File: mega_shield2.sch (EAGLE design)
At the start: 36 parts, among them IC1 L298, IC2 LM2937ET-5V, J2 Mega R3, M1_M2 1X2-3.5MM, M3_M4 1X2-3.5MM

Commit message: Added 6 pin motor headers
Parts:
- removed M1_M2, M3_M4: 1X2-3.5MM, adafruit:1X2-3.5MM
- added JP1: MOTOR1_HEADER, adafruit:PINHD-1X6
- added JP2: MOTOR2_HEADER, adafruit:PINHD-1X6
- 12V_SWITCH: value (none) -> 12V_SWITCH
- renumbered S1 to 12V_SWITCH
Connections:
- removed net N$1: J2.2, R5.2
- removed net N$2: J2.3, R6.2
- new net MEGA2: J2.2, JP1.6, R5.2
- new net MEGA3: J2.3, JP1.5, R6.2
- net GND: now also JP1.3, JP2.3
- net MEGA18: now also JP2.6
- net MEGA19: now also JP2.5
- net MEGA_5V: now also JP1.4, JP2.4
- net MOT1: now also JP1.1; no longer M1_M2.1
- net MOT2: now also JP1.2; no longer M1_M2.2
- net MOT3: now also JP2.1; no longer M3_M4.1
- net MOT4: now also JP2.2; no longer M3_M4.2
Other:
- note added: "1/8/18: CHECK MOTOR HEADER WIRING!!!"
- moved on the sheet: R3, R4, R5, R6

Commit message: Added restricts to ground plane in brd file
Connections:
- net MEGA2: now also JP1.5; no longer JP1.6
- net MEGA3: now also JP1.6; no longer JP1.5
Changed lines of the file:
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@@
 </segment>
 <segment>
-<pinref part="JP1" gate="A" pin="6"/>
-<wire x1="-27.94" y1="-132.08" x2="-17.78" y2="-132.08" width="0.1524" layer="91"/>
-<label x="-17.78" y="-132.08" size="1.778" layer="95"/>
+<pinref part="JP1" gate="A" pin="5"/>
+<wire x1="-27.94" y1="-134.62" x2="-17.78" y2="-134.62" width="0.1524" layer="91"/>
+<label x="-17.78" y="-134.62" size="1.778" layer="95"/>
 </segment>
 </net>
@@
 </segment>
 <segment>
-<pinref part="JP1" gate="A" pin="5"/>
-<wire x1="-27.94" y1="-134.62" x2="-17.78" y2="-134.62" width="0.1524" layer="91"/>
-<label x="-17.78" y="-134.62" size="1.778" layer="95"/>
-</segment>
-</net>
+<pinref part="JP1" gate="A" pin="6"/>
+<wire x1="-27.94" y1="-132.08" x2="-17.78" y2="-132.08" width="0.1524" layer="91"/>
+<label x="-17.78" y="-132.08" size="1.778" layer="95"/>
+</segment>
+</net>

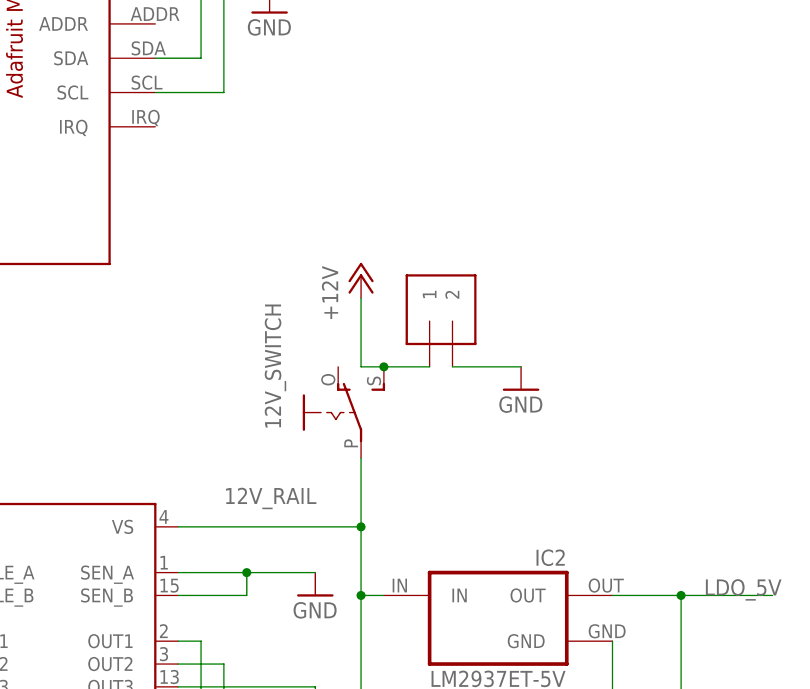
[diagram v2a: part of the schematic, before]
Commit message: Added switch to library, shifted components around on brd
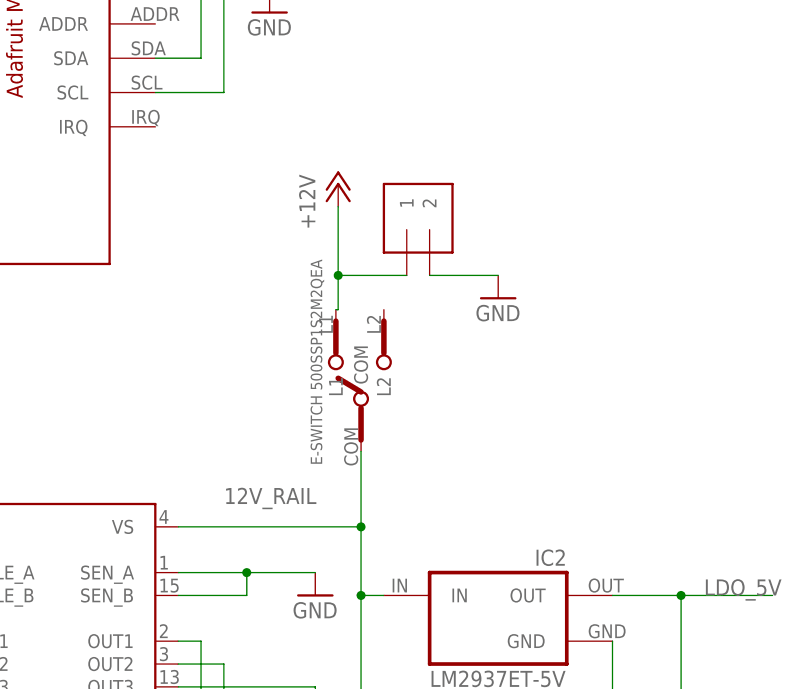
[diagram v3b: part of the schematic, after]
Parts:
- removed 12V_SWITCH: 12V_SWITCH, adafruit:EG1218S
- added U$2: E-SWITCH_500SSP1S2M2QEA, arduinoShield:E-SWITCH_500SSP1S2M2QEA
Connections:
- net +12V: now also U$2.L1; no longer 12V_SWITCH.S
- net 12V_RAIL: now also U$2.COM; no longer 12V_SWITCH.P
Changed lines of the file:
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@@
 <setting verticaltext="up"/>
 </settings>
-<grid distance="0.1" unitdist="inch" unit="inch" style="lines" multiple="1" display="no" altdistance="0.01" altunitdist="inch" altunit="inch"/>
+<grid distance="0.01" unitdist="inch" unit="inch" style="lines" multiple="1" display="no" altdistance="0.01" altunitdist="inch" altunit="inch"/>
 <layers>
 <layer number="1" name="Top" color="4" fill="1" visible="no" active="no"/>
@@
 <part name="GND3" library="supply1" deviceset="GND" device=""/>
 <part name="GND13" library="supply1" deviceset="GND" device=""/>
-<part name="12V_SWITCH" library="adafruit" deviceset="EG1218" device="S" value="12V_SWITCH"/>
 <part name="JP1" library="adafruit" deviceset="PINHD-1X6" device="" value="MOTOR1_HEADER"/>
 <part name="GND14" library="supply1" deviceset="GND" device=""/>
 <part name="JP2" library="adafruit" deviceset="PINHD-1X6" device="" value="MOTOR2_HEADER"/>
 <part name="GND15" library="supply1" deviceset="GND" device=""/>
+<part name="U$2" library="arduinoShield" deviceset="E-SWITCH_500SSP1S2M2QEA" device=""/>
 </parts>
 <sheets>
@@
 <instance part="IC1" gate="L298" x="-27.94" y="-68.58"/>
 <instance part="IC2" gate="G$1" x="22.86" y="-63.5"/>
-<instance part="12V_SW" gate="1" x="7.62" y="-25.4"/>
+<instance part="12V_SW" gate="1" x="5.08" y="-15.24"/>
 <instance part="C2" gate="G$1" x="7.62" y="-76.2"/>
 <instance part="C1" gate="G$1" x="43.18" y="-76.2"/>
@@
 <instance part="S2" gate="1" x="-157.48" y="43.18"/>
 <instance part="R9" gate="G$1" x="-71.12" y="55.88" rot="R180"/>
-<instance part="12V_IN" gate="G$1" x="17.78" y="-30.48" rot="R90"/>
-<instance part="GND2" gate="1" x="25.4" y="-38.1"/>
+<instance part="12V_IN" gate="G$1" x="15.24" y="-20.32" rot="R90"/>
+<instance part="GND2" gate="1" x="22.86" y="-27.94"/>
 <instance part="U$1" gate="G$1" x="-45.72" y="25.4"/>
 <instance part="C4" gate="G$1" x="-2.54" y="11.43"/>
 <instance part="GND3" gate="1" x="-2.54" y="3.81"/>
 <instance part="GND13" gate="1" x="-50.8" y="22.86"/>
-<instance part="12V_SWITCH" gate="1" x="5.08" y="-40.64" smashed="yes">
-<attribute name="NAME" x="-1.27" y="-42.545" size="1.778" layer="95" rot="R90"/>
-</instance>
 <instance part="JP1" gate="A" x="-30.48" y="-137.16" rot="R180"/>
 <instance part="GND14" gate="1" x="-7.62" y="-142.24"/>
 <instance part="JP2" gate="A" x="48.26" y="-137.16" rot="R180"/>
 <instance part="GND15" gate="1" x="71.12" y="-142.24"/>
+<instance part="U$2" gate="G$1" x="1.778" y="-46.482" rot="R90"/>
 </instances>
 <busses>
@@
 <pinref part="12V_IN" gate="G$1" pin="2"/>
 <pinref part="GND2" gate="1" pin="GND"/>
-<wire x1="17.78" y1="-35.56" x2="25.4" y2="-35.56" width="0.1524" layer="91"/>
+<wire x1="15.24" y1="-25.4" x2="22.86" y2="-25.4" width="0.1524" layer="91"/>
 </segment>
 <segment>
@@
 <pinref part="IC1" gate="L298" pin="VS"/>
 <wire x1="-12.7" y1="-53.34" x2="7.62" y2="-53.34" width="0.1524" layer="91"/>
+<label x="-7.62" y="-50.8" size="1.778" layer="95"/>
+<pinref part="U$2" gate="G$1" pin="COM"/>
+<wire x1="7.62" y1="-44.958" x2="7.62" y2="-53.34" width="0.1524" layer="91"/>
 <junction x="7.62" y="-53.34"/>
-<wire x1="7.62" y1="-45.72" x2="7.62" y2="-53.34" width="0.1524" layer="91"/>
-<label x="-7.62" y="-50.8" size="1.778" layer="95"/>
-<pinref part="12V_SWITCH" gate="1" pin="P"/>
 </segment>
 <segment>
@@
 <segment>
 <pinref part="12V_SW" gate="1" pin="+12V"/>
-<wire x1="7.62" y1="-27.94" x2="7.62" y2="-35.56" width="0.1524" layer="91"/>
+<wire x1="5.08" y1="-17.78" x2="5.08" y2="-25.4" width="0.1524" layer="91"/>
 <pinref part="12V_IN" gate="G$1" pin="1"/>
-<wire x1="7.62" y1="-35.56" x2="10.16" y2="-35.56" width="0.1524" layer="91"/>
-<pinref part="12V_SWITCH" gate="1" pin="S"/>
-<wire x1="10.16" y1="-35.56" x2="15.24" y2="-35.56" width="0.1524" layer="91"/>
-<junction x="10.16" y="-35.56"/>
-</segment>
-</net>
+<wire x1="5.08" y1="-25.4" x2="12.7" y2="-25.4" width="0.1524" layer="91"/>
+<pinref part="U$2" gate="G$1" pin="L1"/>
+<wire x1="4.826" y1="-29.21" x2="5.08" y2="-29.21" width="0.1524" layer="91"/>
+<wire x1="5.08" y1="-29.21" x2="5.08" y2="-25.4" width="0.1524" layer="91"/>
+<junction x="5.08" y="-25.4"/>
+</segment>
+</net>

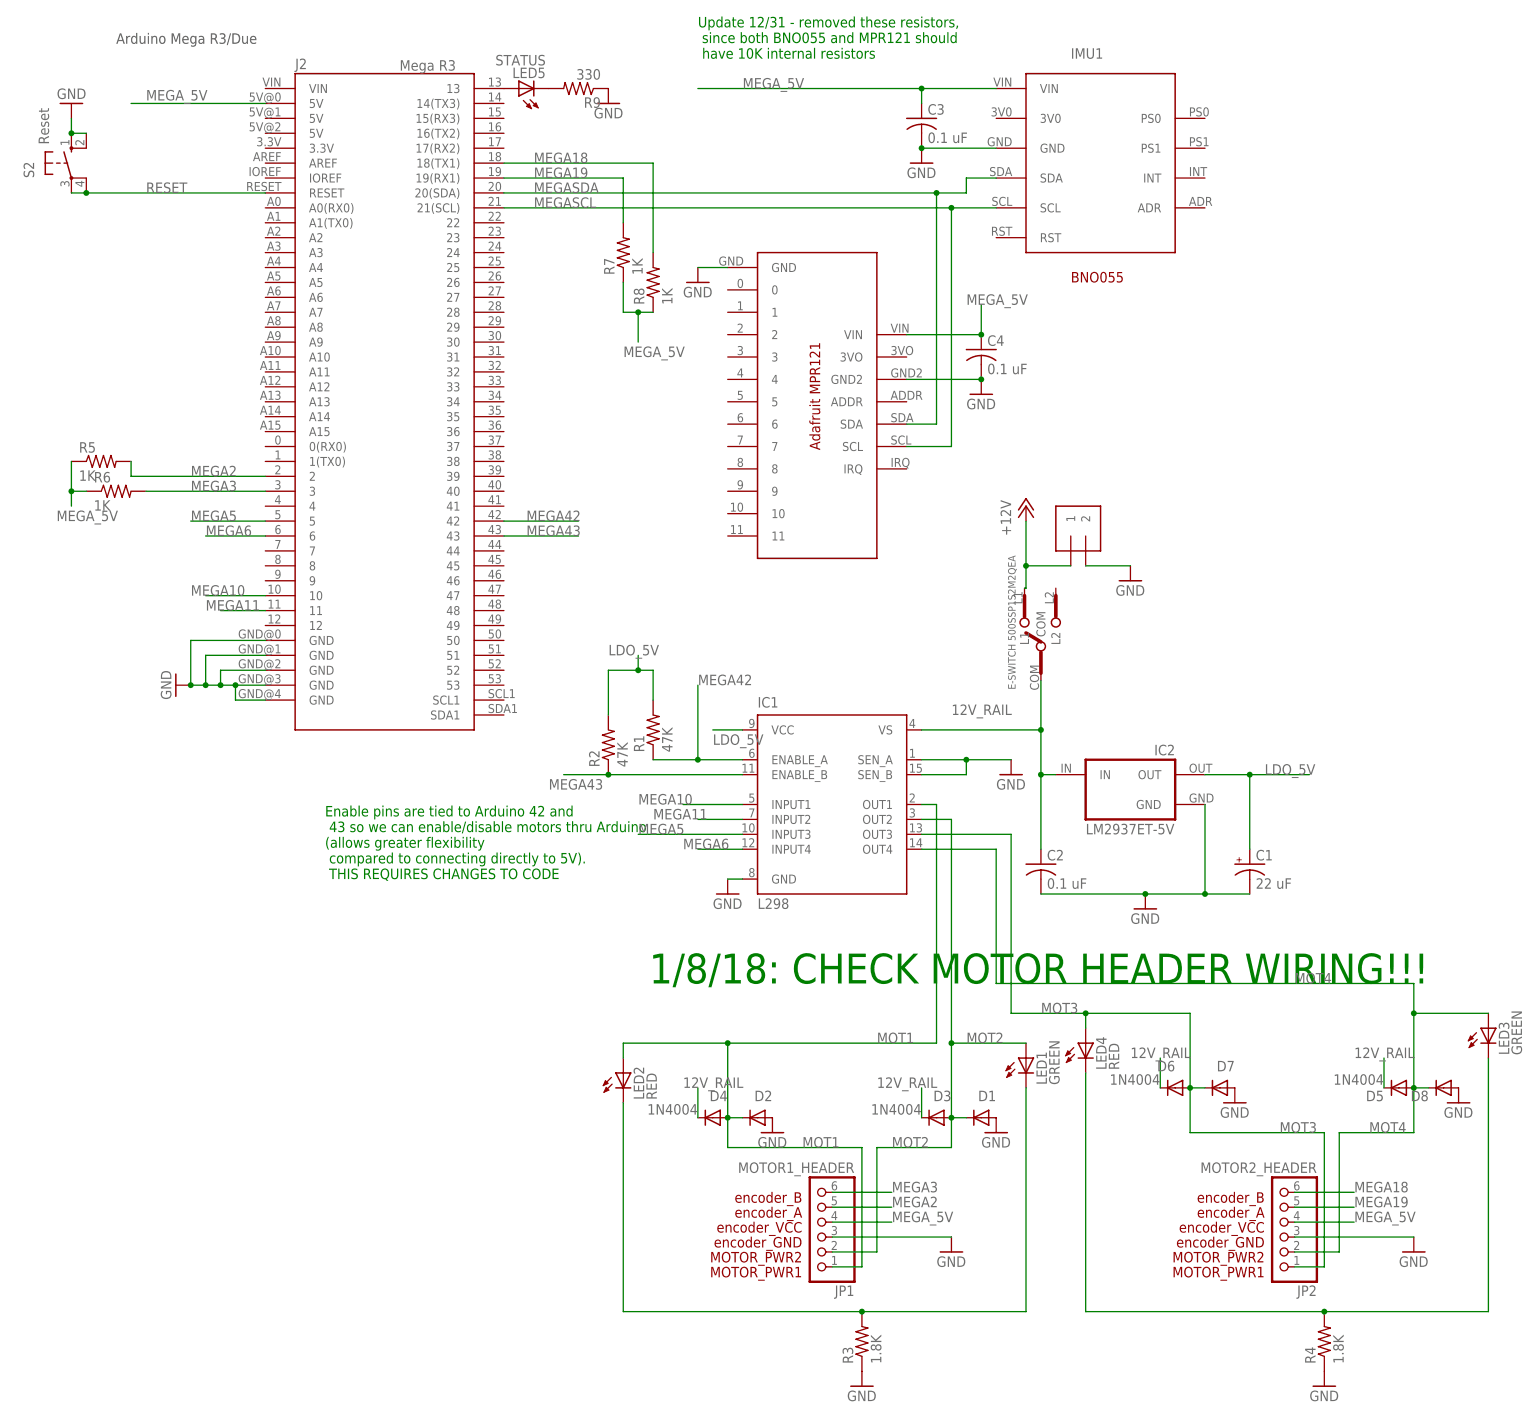
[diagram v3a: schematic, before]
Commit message: added excel component list, changed resistor values
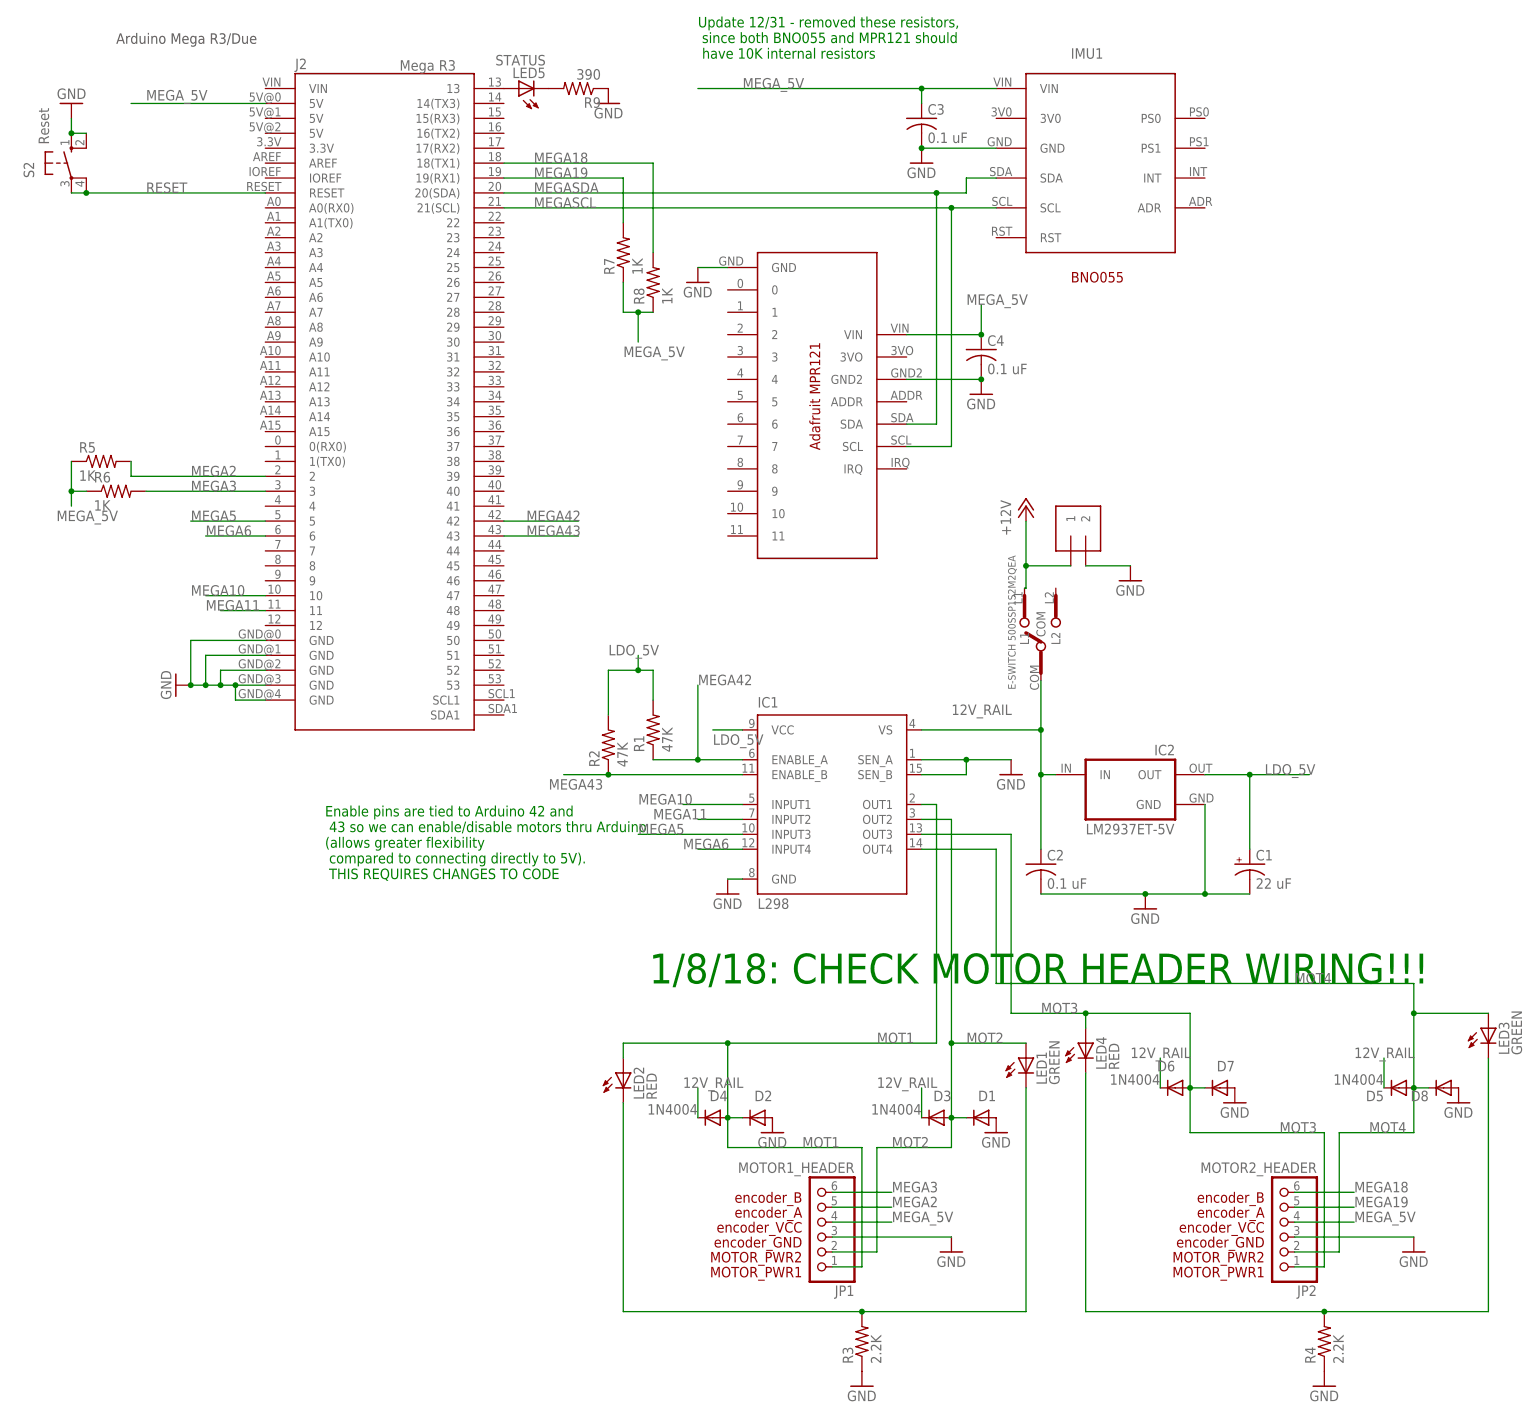
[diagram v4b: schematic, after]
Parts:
- R3, R4: value 1.8K -> 2.2K
- R9: value 330 -> 390
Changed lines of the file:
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@@
 <setting verticaltext="up"/>
 </settings>
-<grid distance="0.01" unitdist="inch" unit="inch" style="lines" multiple="1" display="no" altdistance="0.01" altunitdist="inch" altunit="inch"/>
+<grid distance="0.1" unitdist="inch" unit="inch" style="lines" multiple="1" display="no" altdistance="0.01" altunitdist="inch" altunit="inch"/>
 <layers>
 <layer number="1" name="Top" color="4" fill="1" visible="no" active="no"/>
@@
 <part name="GND8" library="supply1" deviceset="GND" device=""/>
 <part name="LED2" library="adafruit" deviceset="LED" device="3MM" value="RED"/>
-<part name="R3" library="rcl" deviceset="R-US_" device="0207/10" value="1.8K"/>
+<part name="R3" library="rcl" deviceset="R-US_" device="0207/10" value="2.2K"/>
 <part name="GND9" library="supply1" deviceset="GND" device=""/>
 <part name="D5" library="diode" deviceset="1N4004" device=""/>
@@
 <part name="GND11" library="supply1" deviceset="GND" device=""/>
 <part name="LED4" library="adafruit" deviceset="LED" device="3MM" value="RED"/>
-<part name="R4" library="rcl" deviceset="R-US_" device="0207/10" value="1.8K"/>
+<part name="R4" library="rcl" deviceset="R-US_" device="0207/10" value="2.2K"/>
 <part name="GND12" library="supply1" deviceset="GND" device=""/>
 <part name="C3" library="rcl" deviceset="C-US" device="025-050X050" value="0.1 uF"/>
 <part name="LED5" library="adafruit" deviceset="LED" device="3MM" value="STATUS"/>
 <part name="S2" library="switch-omron" deviceset="10-XX" device="" value="Reset"/>
-<part name="R9" library="rcl" deviceset="R-US_" device="0207/10" value="330"/>
+<part name="R9" library="rcl" deviceset="R-US_" device="0207/10" value="390"/>
 <part name="12V_IN" library="adafruit" deviceset="1X2" device="-3.5MM"/>
 <part name="GND2" library="supply1" deviceset="GND" device=""/>
